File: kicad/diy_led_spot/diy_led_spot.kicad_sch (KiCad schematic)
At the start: 15 parts, among them U1 DCDCStepDown, U2 PT4115, U3 ESP32-C3_SUPERMINI_SMD

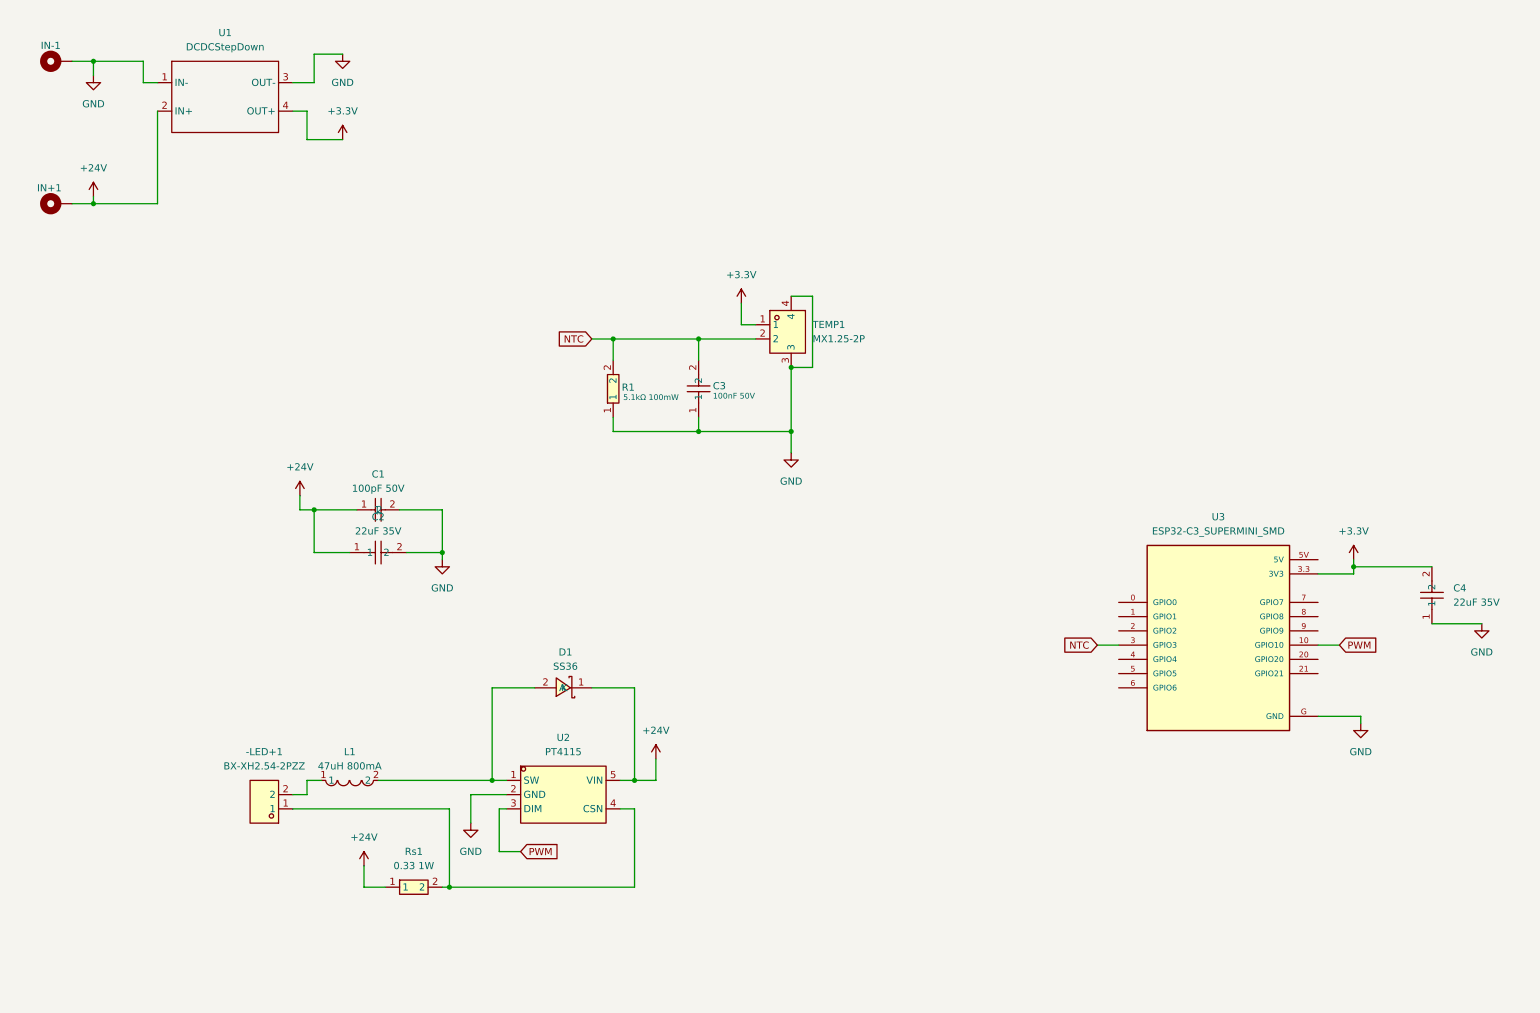
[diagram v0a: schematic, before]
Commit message: kicad: save current PCB/schematic state including routed and step3 variants
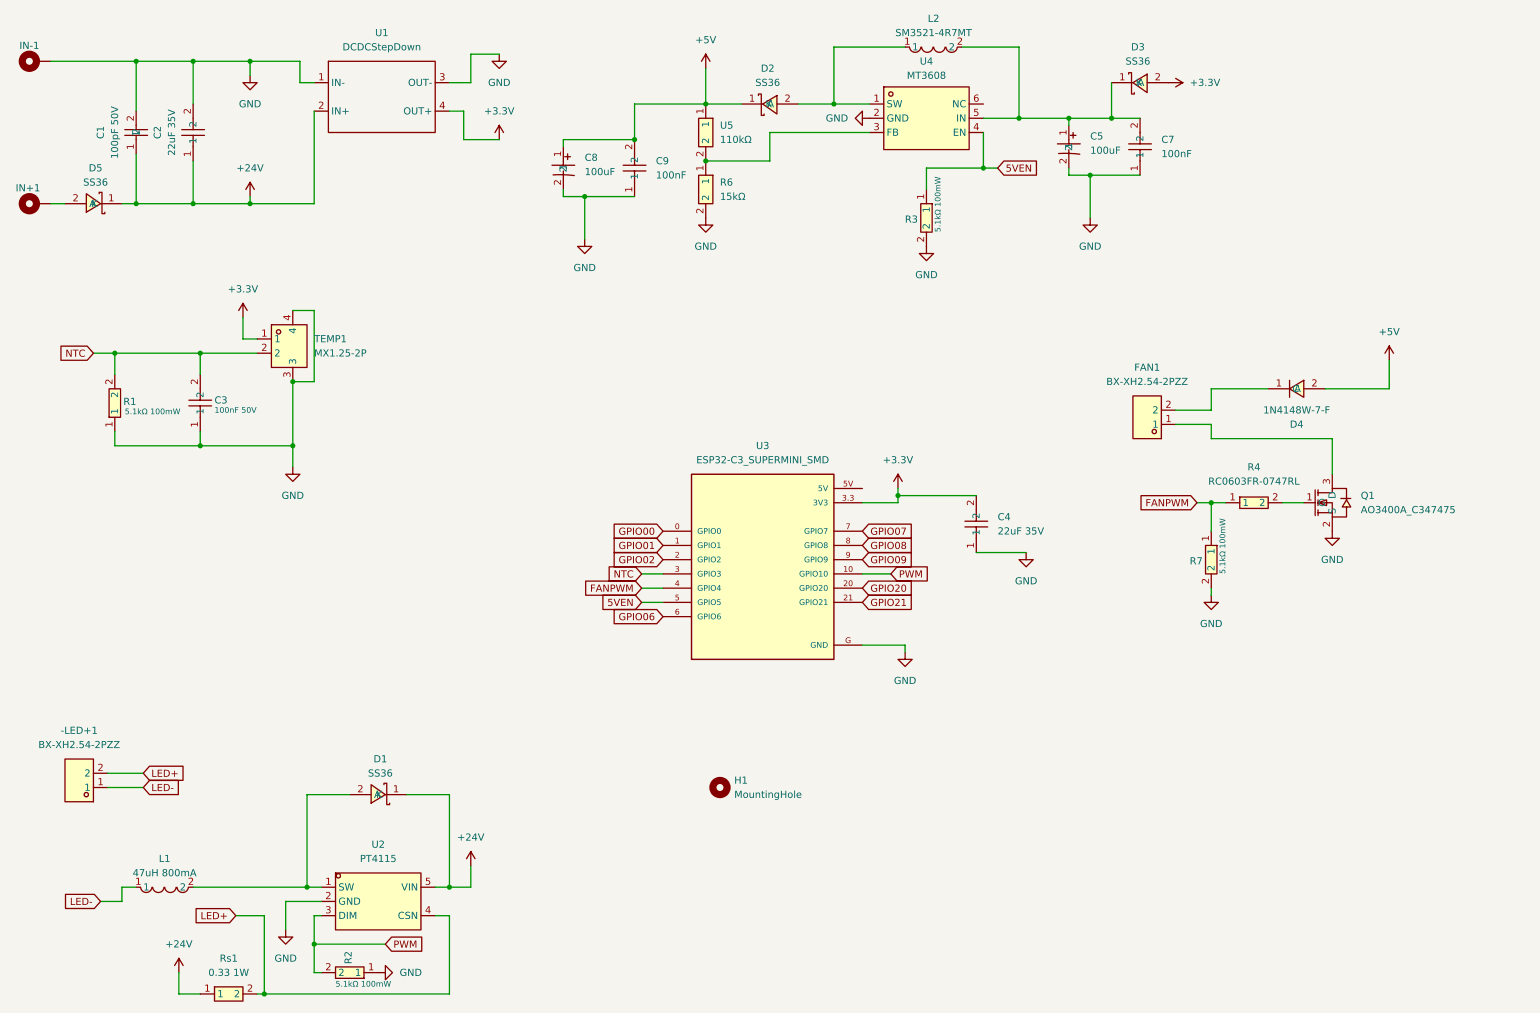
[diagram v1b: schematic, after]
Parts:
- added C5, C8: 100uF, easyeda2kicad:CAP-SMD_BD5.0-L5.3-W5.3-LS6.3-FD, symbol easyeda2kicad:RVT1A101M0505
- added C7, C9: 100nF, easyeda2kicad:C0402, symbol easyeda2kicad:CL05B104KB54PNC
- added D2, D3, D5: SS36, easyeda2kicad:SMA_L4.3-W2.6-LS5.2-RD, symbol easyeda2kicad:SS36
- added D4: 1N4148W-7-F, easyeda2kicad:SOD-123_L2.7-W1.6-LS3.7-RD-1, symbol easyeda2kicad:1N4148W-7-F
- added FAN1: BX-XH2.54-2PZZ, easyeda2kicad:CONN-TH_2P-P2.50_BX-XH2.54-2PZZ, symbol easyeda2kicad:BX-XH2.54-2PZZ
- added H1: MountingHole, symbol Mechanical:MountingHole
- added L2: SM3521-4R7MT, easyeda2kicad:IND-SMD_L3.5-W3.0, symbol easyeda2kicad:SM3521-4R7MT
- added Q1: AO3400A_C347475, easyeda2kicad:SOT-23-3_L2.9-W1.3-P1.90-LS2.4-BR, symbol easyeda2kicad:AO3400A_C347475
- added R2, R3, R7: 5.1kΩ 100mW, easyeda2kicad:R0603, symbol easyeda2kicad:0603WAF5101T5E
- added R4: RC0603FR-0747RL, easyeda2kicad:R0603, symbol easyeda2kicad:RC0603FR-0747RL
- added R6: 15kΩ, easyeda2kicad:R0603, symbol easyeda2kicad:FRC0603F1502TS
- added U4: MT3608, easyeda2kicad:SOT-23-6_L2.9-W1.6-P0.95-LS2.8-BL, symbol easyeda2kicad:MT3608
- added U5: 110kΩ, easyeda2kicad:R0603, symbol easyeda2kicad:FRC0603F1103TS
- -LED+1, TEMP1, U1, U3: now left out of the parts list
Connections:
- net +24V: now also D5.1 (K); no longer IN+1.1
- net +3.3V: now also D3.2 (A)
- net GND: now also C5.2, C7.1, C8.2, C9.1, Q1.2 (S), R2.1, R3.2, R6.2, R7.2, U4.2 (GND)
- net PWM: now also R2.2
- net LED+: now reaches Rs1.2, U2.4 (CSN)
- net LED+: now also -LED+1.2; no longer -LED+1.1
- net LED-: now reaches L1.1
- net LED-: now also -LED+1.1; no longer -LED+1.2
- net GPIO00: now reaches U3.0 (GPIO0)
- net GPIO01: now reaches U3.1 (GPIO1)
- net GPIO02: now reaches U3.2 (GPIO2)
- net GPIO20: now reaches U3.20 (GPIO20)
- net GPIO21: now reaches U3.21 (GPIO21)
- net FANPWM: now reaches U3.4 (GPIO4)
- net FANPWM: now also R4.1, R7.1
- net 5VEN: now reaches U3.5 (GPIO5)
- net 5VEN: now also R3.1, U4.4 (EN)
- net GPIO06: now reaches U3.6 (GPIO6)
- net GPIO07: now reaches U3.7 (GPIO7)
- net GPIO08: now reaches U3.8 (GPIO8)
- net GPIO09: now reaches U3.9 (GPIO9)
- new net: FAN1.1, Q1.3 (D)
- new net: D4.1 (C), FAN1.2
- new net: R6.1, U4.3 (FB), U5.2
- new net: D5.2 (A), IN+1.1
- new net: C5.1, C7.2, D3.1 (K), L2.2, U4.5 (IN)
- new net: D2.2 (A), L2.1, U4.1 (SW)
- new net: Q1.1 (G), R4.2
- new net +5V: C8.1, C9.2, D2.1 (K), D4.2 (A), U5.1
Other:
- moved on the sheet: -LED+1, C1, C2, C3, C4, D1, IN+1, IN-1, L1, R1, Rs1, TEMP1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

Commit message: kicad: save current PCB/schematic state
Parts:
- removed H1: MountingHole, symbol Mechanical:MountingHole
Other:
- moved on the sheet: C1, C2, C3, C4, C5, C7, C8, C9, D2, D3, D4, D5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

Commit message: kicad: save current PCB/schematic state
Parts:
- removed D4: 1N4148W-7-F, easyeda2kicad:SOD-123_L2.7-W1.6-LS3.7-RD-1, symbol easyeda2kicad:1N4148W-7-F
- removed TEMP1: MX1.25-2P, easyeda2kicad:CONN-SMD_2P-P1.25_XUNPU_WAFER-MX1.25-2PWB, symbol easyeda2kicad:WAFER-MX1.25-2PWB
- added D4: SS36, easyeda2kicad:SMA_L4.3-W2.6-LS5.2-RD, symbol easyeda2kicad:SS36
- added TEMP1: BX-XH2.54-2PZZ, easyeda2kicad:CONN-TH_2P-P2.50_BX-XH2.54-2PZZ, symbol easyeda2kicad:BX-XH2.54-2PZZ
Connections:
- net +3.3V: now also TEMP1.1
- net +5V: now also D4.2 (A)
- net NTC: now also TEMP1.2
- net at FAN1.2: now also D4.1 (K)
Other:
- moved on the sheet: C4

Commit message: kicad: save current PCB/schematic state
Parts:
- renumbered U5 to R5
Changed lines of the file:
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@@
 		(dnp no)
 		(fields_autoplaced yes)
-		(property "Reference" "U5"
+		(property "Reference" "R5"
 			(at 179.07 38.0999 90)
 			(effects
@@
 			(project ""
 				(path "/4fa70a5f-0d1c-4a8c-b3fc-6044dfefb6dd"
-					(reference "U5")
+					(reference "R5")
 					(unit 1)
 				)
